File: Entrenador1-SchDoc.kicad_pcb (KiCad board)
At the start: 2 copper layers, 154.9 x 106.7 mm, 88 parts, among them J11 CON8, J3 ICSP, J5 CON8, J6 CON8, J7 CON8, J9 3vias, P1 CONN_01X04, P10 CONN_01X04, P2 CONN_01X04, P3 CONN_01X05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

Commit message: Bugs en PCNEW
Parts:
- moved S3 0.76 mm to (84.4, 90.3)
- moved S4 0.58 mm to (71.7, 90.3)
- moved S5 0.15 mm to (89.0, 124.5)
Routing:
- net GND: track 734.1 -> 735.7 mm
- net /Display_D: track 38.0 -> 38.9 mm
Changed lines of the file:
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@@
     (links 235)
     (no_connects 13)
-    (area 65.989999 32.969999 221.030001 139.750001)
+    (area 64.225 32.969999 230.290572 148.75)
     (thickness 1.6)
     (drawings 96)
@@
   )
   (module libreria:SW_PUSH_6mm_h13mm (layer F.Cu)
-    (at 88.955 124.31 270)
+    (at 88.955 124.46 270)
     (descr "tactile push button, 6x6mm e.g. PHAP33xx series, height=13mm")
     (tags "tact sw push 6mm")
@@
   )
   (module libreria:SW_PUSH_6mm_h13mm (layer F.Cu)
-    (at 71.12 90.32 90)
+    (at 71.7 90.32 90)
     (descr "tactile push button, 6x6mm e.g. PHAP33xx series, height=13mm")
     (tags "tact sw push 6mm")
@@
   )
   (module libreria:SW_PUSH_6mm_h13mm (layer F.Cu)
-    (at 83.82 90.805 90)
+    (at 84.4 90.32 90)
     (descr "tactile push button, 6x6mm e.g. PHAP33xx series, height=13mm")
     (tags "tact sw push 6mm")
@@
   (segment (start 114.935 89.535) (end 114.935 85.725) (width 0.635) (layer B.Cu) (net 11))
   (segment (start 121.92 100.33) (end 121.92 87.63) (width 0.635) (layer B.Cu) (net 11))
+  (segment (start 110.49 81.915) (end 108.585 80.01) (width 0.8) (layer B.Cu) (net 12))
+  (segment (start 108.585 80.01) (end 79.43 80.01) (width 0.8) (layer B.Cu) (net 12))
+  (segment (start 88.9 85.09) (end 88.9 83.82) (width 0.8) (layer B.Cu) (net 12))
+  (segment (start 79.43 80.01) (end 75.62 83.82) (width 0.8) (layer B.Cu) (net 12))
+  (segment (start 75.62 83.82) (end 78.16 86.36) (width 0.8) (layer B.Cu) (net 12))
+  (segment (start 78.16 86.36) (end 87.63 86.36) (width 0.8) (layer B.Cu) (net 12))
+  (segment (start 87.63 86.36) (end 88.9 85.09) (width 0.8) (layer B.Cu) (net 12))
   (segment (start 176.403 64.389) (end 176.703 64.389) (width 0.8) (layer B.Cu) (net 12))
   (segment (start 176.703 64.389) (end 177.953 65.639) (width 0.8) (layer B.Cu) (net 12))
@@
   (segment (start 112.53363 96.52) (end 112.395 96.52) (width 0.8) (layer B.Cu) (net 12))
   (segment (start 113.80363 95.25) (end 112.53363 96.52) (width 0.8) (layer B.Cu) (net 12))
-  (segment (start 79.43 80.01) (end 108.585 80.01) (width 0.8) (layer B.Cu) (net 12))
-  (segment (start 108.585 80.01) (end 110.49 81.915) (width 0.8) (layer B.Cu) (net 12))
-  (segment (start 75.62 83.82) (end 79.43 80.01) (width 0.8) (layer B.Cu) (net 12))
   (segment (start 92.072208 134.62) (end 103.502208 123.19) (width 0.8) (layer B.Cu) (net 12))
   (segment (start 103.502208 123.19) (end 106.045 123.19) (width 0.8) (layer B.Cu) (net 12))
@@
   (segment (start 106.553 60.833) (end 106.553 62.23) (width 0.8) (layer B.Cu) (net 12))
   (segment (start 75.62 90.32) (end 71.755 94.185) (width 0.8) (layer B.Cu) (net 12))
-  (segment (start 75.62 83.82) (end 78.16 86.36) (width 0.8) (layer B.Cu) (net 12))
-  (segment (start 86.265 86.36) (end 87.320001 85.304999) (width 0.8) (layer B.Cu) (net 12))
-  (segment (start 78.16 86.36) (end 86.265 86.36) (width 0.8) (layer B.Cu) (net 12))
-  (segment (start 87.320001 85.304999) (end 88.32 84.305) (width 0.8) (layer B.Cu) (net 12))
   (segment (start 212.217 38.72337) (end 211.798001 39.142369) (width 0.8) (layer B.Cu) (net 12))
   (segment (start 211.798001 39.142369) (end 211.798001 39.413614) (width 0.8) (layer B.Cu) (net 12))
@@
   (segment (start 101.473 62.23) (end 101.473 68.072) (width 0.635) (layer B.Cu) (net 40) (status 20))
   (segment (start 104.013 62.23) (end 104.013 68.072) (width 0.635) (layer B.Cu) (net 41) (status 20))
-  (segment (start 83.82 90.805) (end 83.82 89.916) (width 0.635) (layer B.Cu) (net 42))
-  (segment (start 83.82 89.916) (end 85.09 88.646) (width 0.635) (layer B.Cu) (net 42))
-  (segment (start 85.09 88.646) (end 91.7194 88.646) (width 0.635) (layer B.Cu) (net 42))
-  (segment (start 91.7194 88.646) (end 92.71 89.6366) (width 0.635) (layer B.Cu) (net 42))
-  (segment (start 92.71 89.6366) (end 92.71 90.805) (width 0.635) (layer B.Cu) (net 42))
-  (segment (start 83.185 95.25) (end 83.185 91.44) (width 0.635) (layer B.Cu) (net 42))
-  (segment (start 83.185 91.44) (end 83.82 90.805) (width 0.635) (layer B.Cu) (net 42))
+  (segment (start 83.185 95.25) (end 83.185 91.535) (width 0.635) (layer B.Cu) (net 42))
+  (segment (start 83.185 91.535) (end 84.4 90.32) (width 0.635) (layer B.Cu) (net 42))
+  (segment (start 92.71 90.805) (end 92.71 89.6366) (width 0.635) (layer B.Cu) (net 42))
+  (segment (start 92.71 89.6366) (end 91.3384 88.265) (width 0.635) (layer B.Cu) (net 42))
+  (segment (start 91.3384 88.265) (end 86.455 88.265) (width 0.635) (layer B.Cu) (net 42))
+  (segment (start 86.455 88.265) (end 84.4 90.32) (width 0.635) (layer B.Cu) (net 42))
   (segment (start 71.12 83.82) (end 71.755 83.82) (width 0.635) (layer B.Cu) (net 43))
   (segment (start 71.755 83.82) (end 75.692 87.757) (width 0.635) (layer B.Cu) (net 43))
@@
   (segment (start 209.169 53.848) (end 211.074 53.848) (width 0.5) (layer B.Cu) (net 59))
   (segment (start 211.074 53.848) (end 213.868 56.642) (width 0.5) (layer B.Cu) (net 59))
+  (segment (start 204.382766 61.507766) (end 204.382766 62.317234) (width 0.5) (layer B.Cu) (net 60))
+  (segment (start 211.074 45.593) (end 211.074 45.72) (width 0.5) (layer B.Cu) (net 60))
+  (segment (start 209.169 43.688) (end 211.074 45.593) (width 0.5) (layer B.Cu) (net 60))
+  (segment (start 211.074 45.72) (end 211.074 51.308) (width 0.5) (layer B.Cu) (net 60))
+  (segment (start 212.217 45.72) (end 211.08563 45.72) (width 0.5) (layer B.Cu) (net 60))
+  (segment (start 211.08563 45.72) (end 211.074 45.72) (width 0.5) (layer B.Cu) (net 60))
   (segment (start 215.099989 55.333989) (end 215.099989 57.823011) (width 0.5) (layer B.Cu) (net 60))
   (segment (start 212.454999 60.468001) (end 211.455 61.468) (width 0.5) (layer B.Cu) (net 60))
   (segment (start 215.099989 57.823011) (end 212.454999 60.468001) (width 0.5) (layer B.Cu) (net 60))
-  (segment (start 211.074 45.593) (end 211.074 51.308) (width 0.5) (layer B.Cu) (net 60))
-  (segment (start 209.169 43.688) (end 211.074 45.593) (width 0.5) (layer B.Cu) (net 60))
   (segment (start 211.415234 61.507766) (end 211.455 61.468) (width 0.5) (layer F.Cu) (net 60))
   (segment (start 211.074 51.308) (end 215.099989 55.333989) (width 0.5) (layer B.Cu) (net 60))
   (segment (start 204.382766 61.507766) (end 211.415234 61.507766) (width 0.5) (layer F.Cu) (net 60))
   (via (at 211.455 61.468) (size 2) (drill 0.635) (layers F.Cu B.Cu) (net 60))
-  (segment (start 204.557234 61.507766) (end 204.382766 61.507766) (width 0.5) (layer B.Cu) (net 60))
-  (segment (start 204.382766 62.317234) (end 204.382766 61.507766) (width 0.5) (layer B.Cu) (net 60))
   (via (at 204.382766 61.507766) (size 2) (drill 0.635) (layers F.Cu B.Cu) (net 60))
-  (segment (start 204.597 61.468) (end 204.557234 61.507766) (width 0.5) (layer B.Cu) (net 60))
   (segment (start 198.628 68.072) (end 204.382766 62.317234) (width 0.5) (layer B.Cu) (net 60))
   (segment (start 206.248 68.072) (end 209.804 64.516) (width 0.5) (layer B.Cu) (net 61))

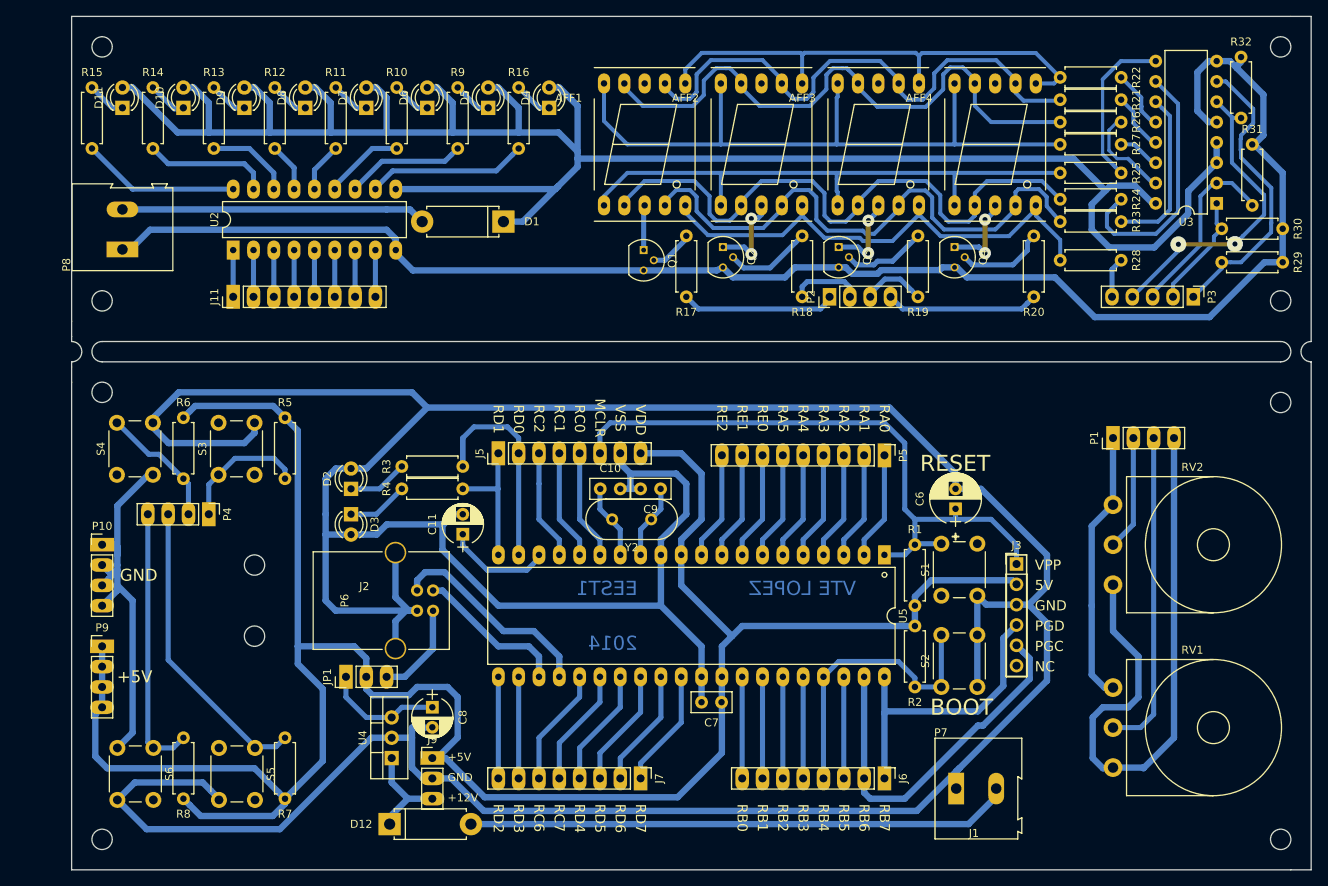
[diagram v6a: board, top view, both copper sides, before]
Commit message: se cambia de posición el teclado
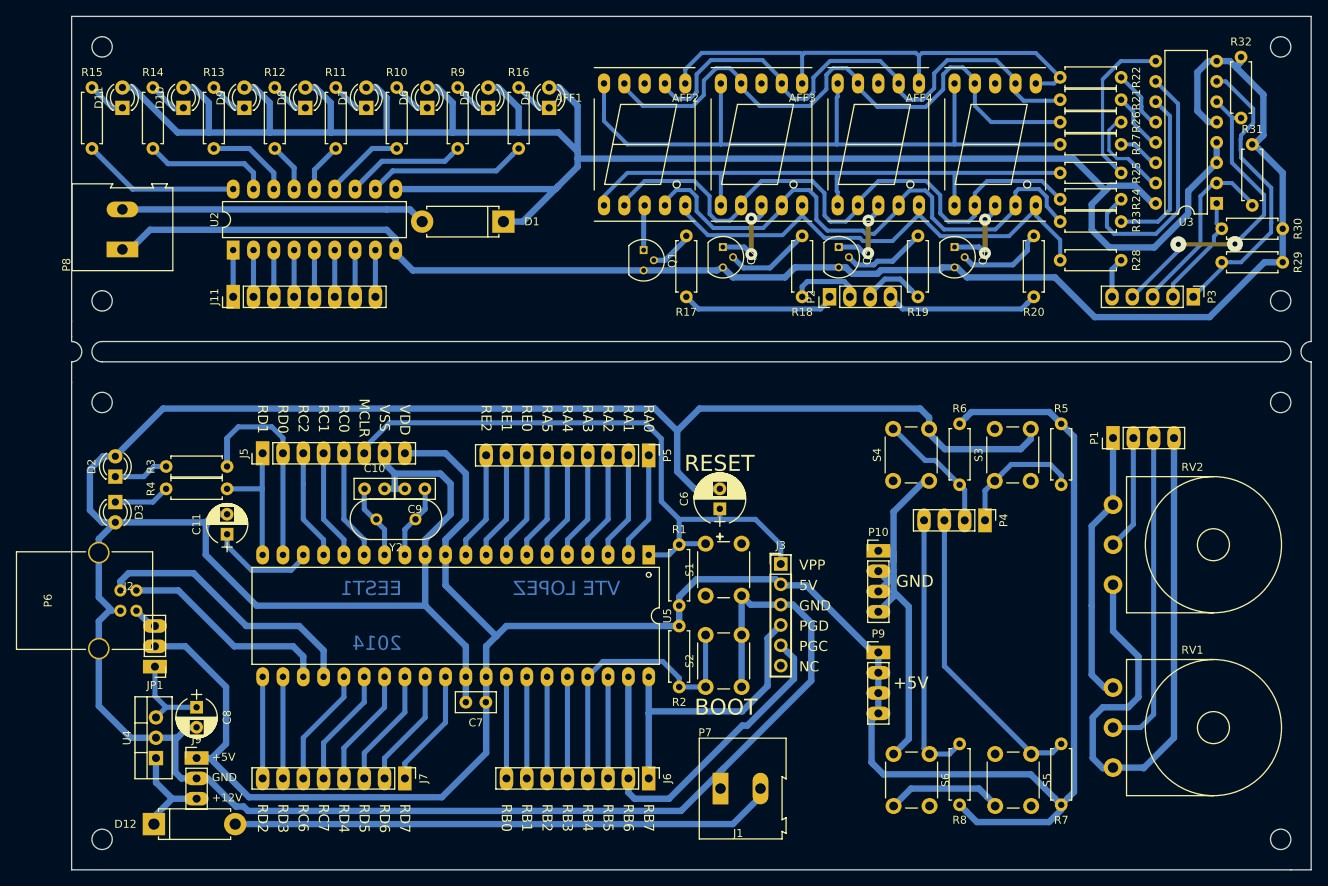
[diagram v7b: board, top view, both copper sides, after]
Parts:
- moved R5 97.0 mm to (189.7, 83.9)
- moved R6 97.0 mm to (177.0, 83.9)
- moved R7 97.0 mm to (189.7, 131.6)
- moved R8 97.0 mm to (177.0, 131.6)
- moved S4 97.0 mm to (168.7, 91.1)
- moved S5 97.0 mm to (186.0, 125.2)
- moved P10 97.0 mm to (166.9, 99.8)
- moved P4 97.0 mm to (180.2, 96.0)
- moved P9 97.0 mm to (166.9, 112.5)
- moved S3 97.0 mm to (181.4, 91.1)
- moved S6 97.0 mm to (173.3, 125.2)
- moved P6 37.1 mm to (74.1, 107.3)
- moved D2 29.5 mm to (71.5, 90.6)
- moved D3 29.5 mm to (71.5, 93.7)
- moved P7 29.5 mm to (147.1, 129.5)
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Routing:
- net GND: track 735.7 -> 668.8 mm
- net +5VUSB: track 12.0 -> 2.56 mm
- net RC5: track 26.4 -> 34.3 mm
- net RC4: track 19.2 -> 26.8 mm
- net Net-(C8-Pad1): track 14.9 -> 11.3 mm
- net MCRL: track 81.0 -> 79.6 mm
- net VDD: track 541.3 -> 542.1 mm
- net Net-(D2-Pad1): track 7.51 -> 6.88 mm
- net Net-(D3-Pad1): track 7.67 -> 7.03 mm
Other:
- outline, holes or cut-outs redrawn

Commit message: Diseño definitivo con desplazamiento USB
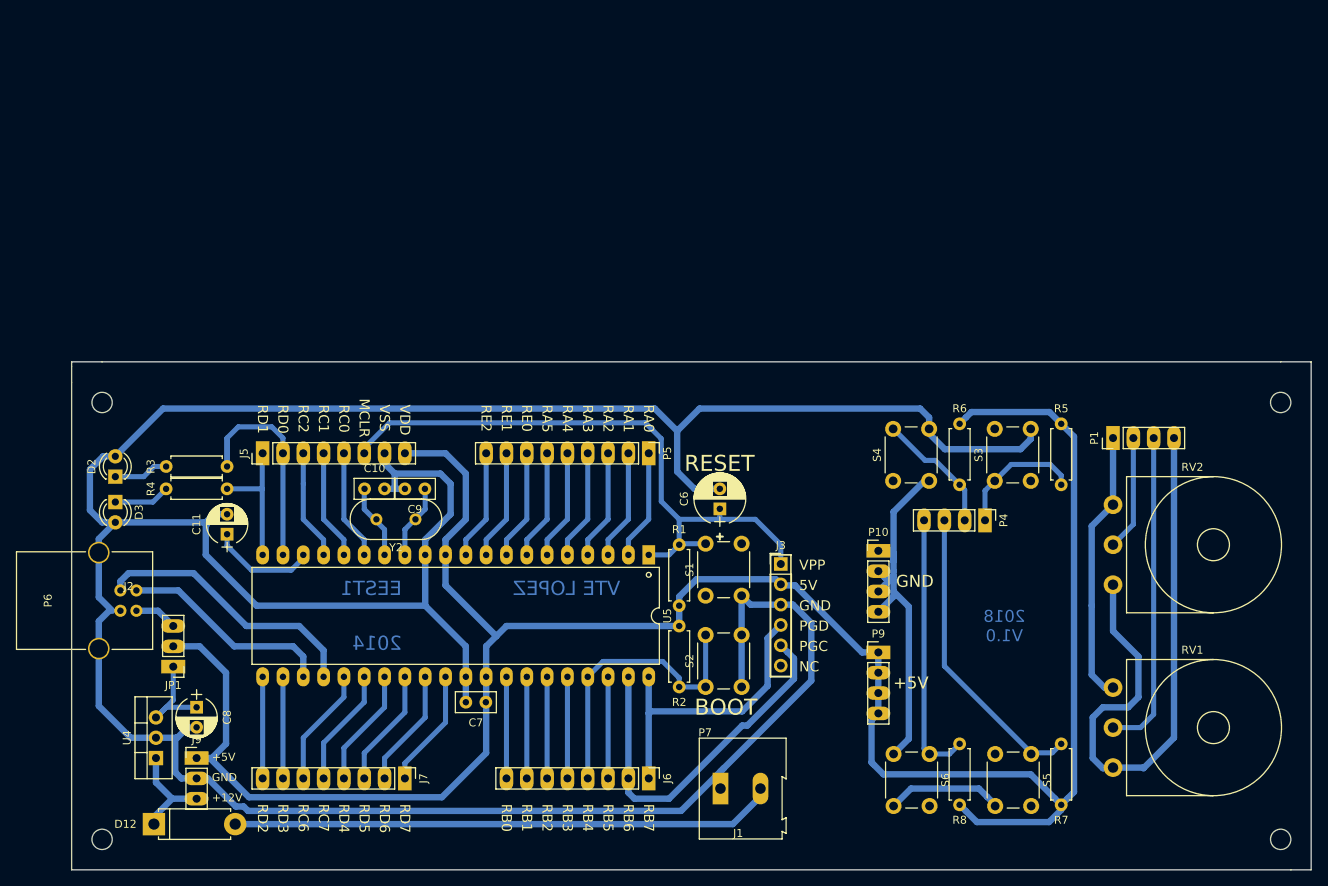
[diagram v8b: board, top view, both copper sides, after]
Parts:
- removed AFF1, AFF2, AFF3, AFF4: 7SEGMENTS, libreria:7SegmentLED_LTS6760_LTS6780
- removed D1: 1n4004, libreria:D_5W_P10.16mm_Horizontal
- removed D10, D11, D4, D5, D6, D7, D8, D9: LED, libreria:LED_D3.0mm
- removed J11: CON8, libreria:Socket_Strip_Straight_1x08_Pitch2.54mm
- removed P2: CONN_01X04, libreria:Socket_Strip_Straight_1x04_Pitch2.54mm
- removed P3: CONN_01X05, libreria:Socket_Strip_Straight_1x05_Pitch2.54mm
- removed P8: CONN_01X02, libreria:TerminalBlock_Altech_AK300-2_P5.00mm
- removed Q1, Q2, Q3, Q4: BC548, TO_SOT_Packages_THT:TO-92_Molded_Narrow
- removed R10, R11, R12, R13, R14, R15, R16, R21, R22, R23, R24, R25, R26, R27, R28, R9: 180, libreria:R_Axial_DIN0207_L6.3mm_D2.5mm_P7.62mm_Horizontal
- removed R17, R18, R19, R20: 1200, libreria:R_Axial_DIN0207_L6.3mm_D2.5mm_P7.62mm_Horizontal
- removed R29, R30, R31, R32: 10k, libreria:R_Axial_DIN0207_L6.3mm_D2.5mm_P7.62mm_Horizontal
- removed U2: ULN2803, libreria:DIP-18_W7.62mm_LongPads
- removed U3: 4511, libreria:DIP-16_W7.62mm
- P6: footprint libreria:USB_B -> USB_B
- moved JP1 2.29 mm to (78.7, 114.3)
- moved P5 0.25 mm to (138.2, 87.6)
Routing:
- net VDD: track 542.1 -> 284.0 mm
- net GND: track 668.8 -> 470.1 mm
- net /g: track 85.8 -> 0.00 mm
- net /d: track 76.6 -> 0.00 mm
- net /f: track 75.0 -> 0.00 mm
- net /c: track 72.1 -> 0.00 mm
- net /e: track 71.4 -> 0.00 mm
- net /a: track 68.5 -> 0.00 mm
- net /h: track 63.6 -> 0.00 mm
- net /b: track 61.7 -> 0.00 mm
- net /Display_D: track 38.9 -> 0.00 mm, vias 2 -> 0
- net Net-(D1-Pad2): track 38.1 -> 0.00 mm
- net /Display_A: track 37.7 -> 0.00 mm
- net Net-(R24-Pad1): track 32.0 -> 0.00 mm
- net /Display_C: track 23.6 -> 0.00 mm
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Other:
- board size 154.9 x 106.7 mm -> 154.9 x 63.5 mm
- board text added: "2018 V1.0"
